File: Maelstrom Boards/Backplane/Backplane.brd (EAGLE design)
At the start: 254 x 101.6 mm, 10 parts, among them P3 39-30-04?_S

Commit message: Updated Backplane
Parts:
- added P1: 39-30-02?_S, con-molex-mini-fit:39-30-?02?
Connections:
- net 5V: now also P1.1
- net GND: now also P1.2
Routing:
- net 5V: track 269.1 -> 349.1 mm
- net GND: track 351.8 -> 425.8 mm
- net 3.3V: track 364.8 -> 360.3 mm
- net ROBOT_SCL: track 447.0 -> 442.9 mm
- net PLTA_ON/OFF: track 512.7 -> 515.1 mm, vias 1 -> 2
- net SWITCH_3: track 523.0 -> 521.9 mm
- net SWITCH_2: track 503.2 -> 502.3 mm
- net SWITCH_1: track 500.7 -> 499.9 mm
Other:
- board text added: "SPARE_2"
- board text added: "SPARE_3"
- board text added: "SPARE_4"
- board text added: "SPARE_5"
- board text added: "SPARE_6"
- board text added: "SPARE_7"

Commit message: Updated Backplane
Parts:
- moved P1 0.13 mm to (13.8, 90.7)
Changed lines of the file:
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@@
 <element name="U$3" library="5530843-6" package="5530843-6-BACKPLANEMATE" value="5530843-FEMALE" x="22.86" y="20.32" smashed="yes"/>
 <element name="U$4" library="5530843-6" package="5530843-6-BACKPLANEMATE" value="5530843-FEMALE" x="163.83" y="20.32" smashed="yes"/>
-<element name="P1" library="con-molex-mini-fit" package="39-30-?02?" value="39-30-02?_S" x="13.97" y="90.678" smashed="yes" rot="R270">
-<attribute name="NAME" x="0.2159" y="94.107" size="1.016" layer="25" ratio="18"/>
-<attribute name="VALUE" x="0.2159" y="85.979" size="1.016" layer="27" ratio="10"/>
+<element name="P1" library="con-molex-mini-fit" package="39-30-?02?" value="39-30-02?_S" x="13.843" y="90.678" smashed="yes" rot="R270">
+<attribute name="NAME" x="0.0889" y="94.107" size="1.016" layer="25" ratio="18"/>
+<attribute name="VALUE" x="0.0889" y="85.979" size="1.016" layer="27" ratio="10"/>
 </element>
 </elements>
@@
 <wire x1="73.025" y1="95.06780625" x2="72.31220625" y2="95.7806" width="1.016" layer="16"/>
 <wire x1="72.31220625" y1="95.7806" x2="29.6136" y2="95.7806" width="1.016" layer="16"/>
-<wire x1="21.971" y1="88.138" x2="16.51" y2="88.138" width="1.016" layer="16"/>
-<wire x1="16.51" y1="88.138" x2="13.97" y2="90.678" width="1.016" layer="16"/>
+<wire x1="21.971" y1="88.138" x2="16.383" y2="88.138" width="1.016" layer="16"/>
+<wire x1="16.383" y1="88.138" x2="13.843" y2="90.678" width="1.016" layer="16"/>
 <wire x1="29.6136" y1="95.7806" x2="21.971" y2="88.138" width="1.016" layer="16"/>
 </signal>
@@
 <wire x1="75.819" y1="89.535" x2="75.819" y2="95.758" width="1.016" layer="16"/>
 <wire x1="75.819" y1="95.758" x2="73.533" y2="98.044" width="1.016" layer="16"/>
-<wire x1="73.533" y1="98.044" x2="26.8478" y2="98.044" width="1.016" layer="16"/>
-<wire x1="26.8478" y1="98.044" x2="19.4818" y2="90.678" width="1.016" layer="16"/>
+<wire x1="73.533" y1="98.044" x2="26.7208" y2="98.044" width="1.016" layer="16"/>
+<wire x1="26.7208" y1="98.044" x2="19.3548" y2="90.678" width="1.016" layer="16"/>
 <wire x1="52.197" y1="6.604" x2="61.595" y2="6.604" width="1.016" layer="16"/>
 <via x="61.595" y="6.604" extent="1-16" drill="0.35"/>

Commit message: Updated Backplane
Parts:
- moved U$1 12.7 mm to (104.1, 81.3)
- moved U$3 12.7 mm to (35.6, 20.3)
- moved U$8 11.4 mm to (19.7, 7.37)
- moved U$2 1.27 mm to (231.1, 81.3)
- moved U$4 1.27 mm to (162.6, 20.3)
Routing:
- net GND: track 425.9 -> 458.0 mm
- net SPARE6: track 442.0 -> 423.1 mm
- net 5V: track 349.2 -> 368.1 mm
- net PWM_2: track 312.8 -> 330.8 mm, vias 5 -> 4
- net PWM_1: track 313.1 -> 330.8 mm, vias 5 -> 4
- net SPARE5: track 443.1 -> 425.5 mm
- net KILL_SWITCH: track 502.2 -> 488.1 mm, vias 7 -> 5
- net SWITCH_2: track 502.3 -> 489.2 mm
- net SWITCH_3: track 521.9 -> 509.7 mm
- net SPARE7: track 443.8 -> 432.1 mm
- net SWITCH_1: track 499.9 -> 488.7 mm
- net 3.3V: track 360.3 -> 349.2 mm
- net SWITCH_4: track 508.5 -> 501.0 mm
- net SPARE4: track 417.2 -> 411.3 mm
- net SPARE3: track 413.9 -> 408.5 mm
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
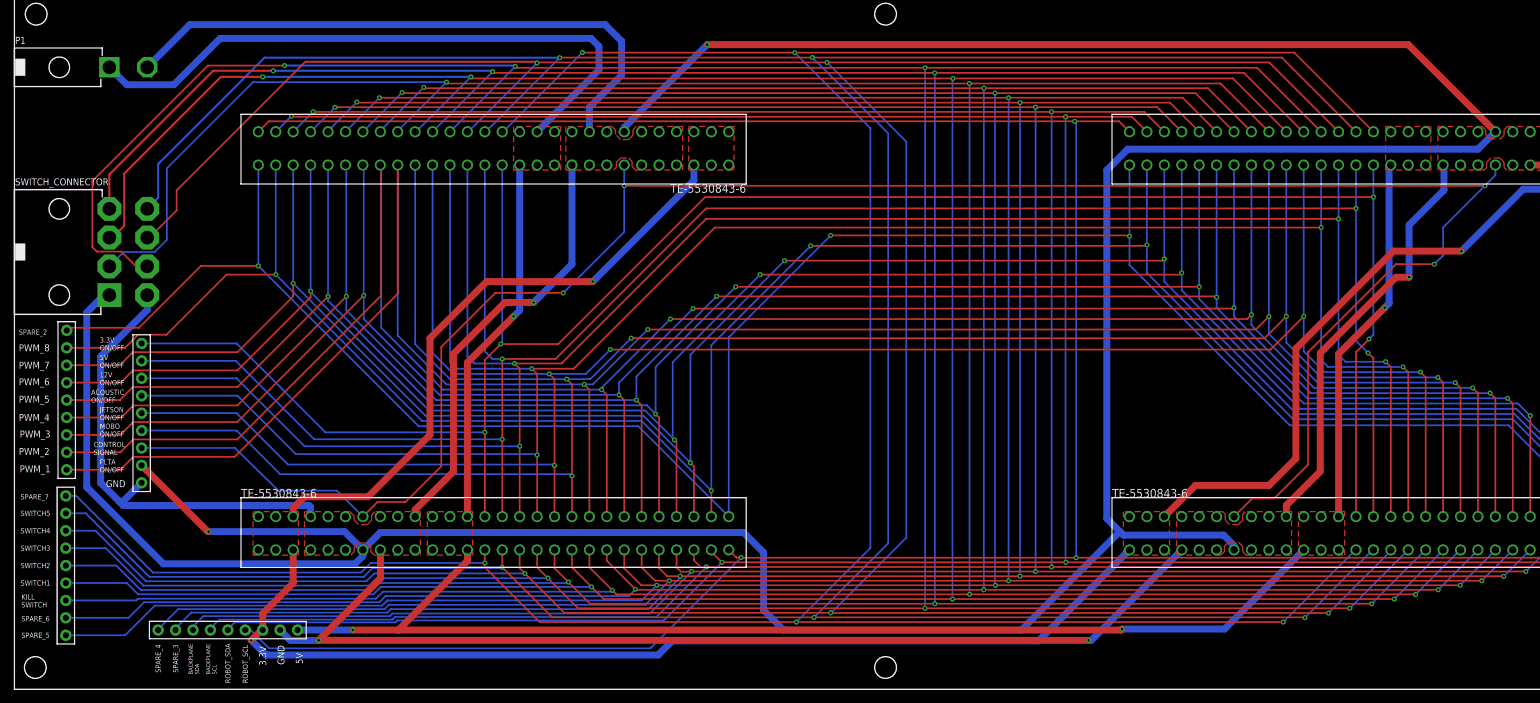
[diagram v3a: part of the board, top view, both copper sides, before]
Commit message: Finished Backplane
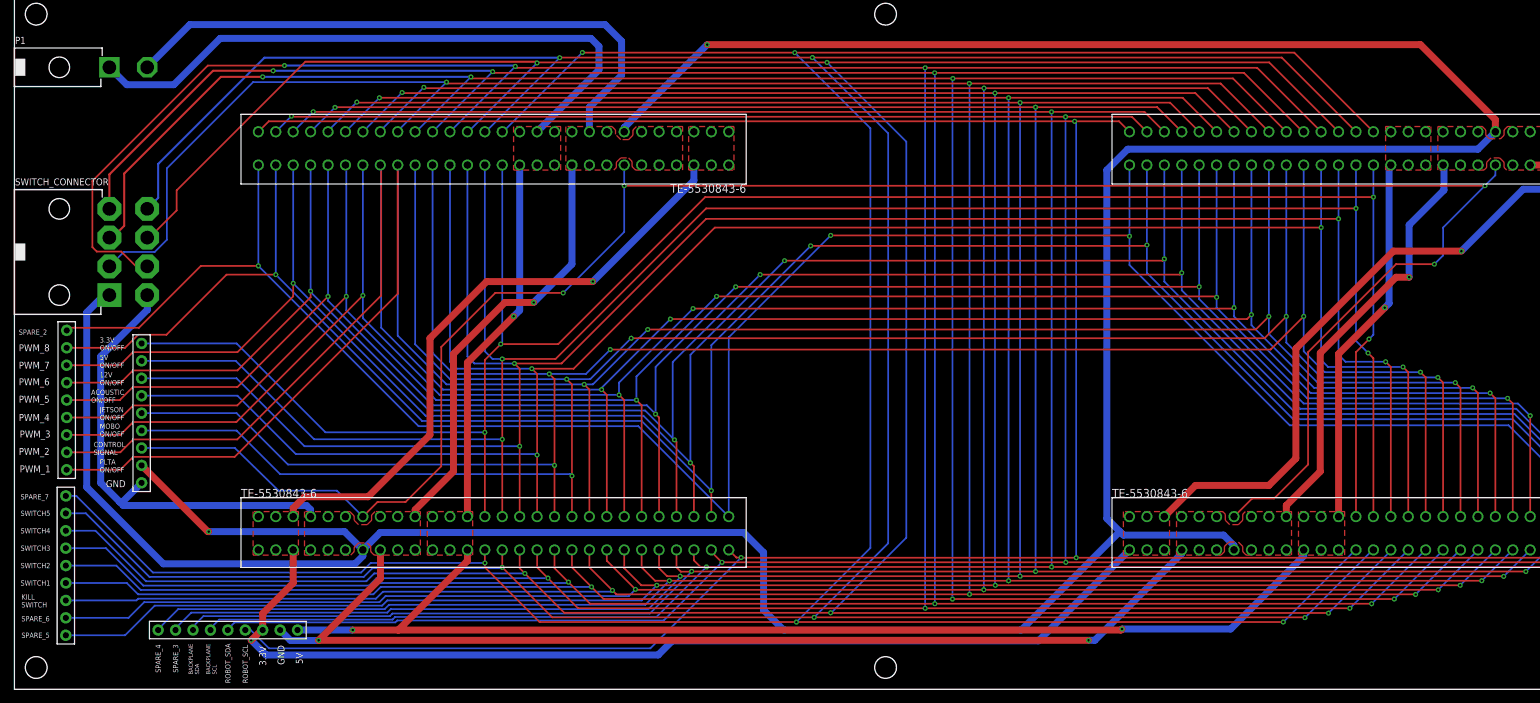
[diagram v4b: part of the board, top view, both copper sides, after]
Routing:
- net PLTA_ON/OFF: track 510.0 -> 511.1 mm
- net 5V: track 368.1 -> 368.6 mm
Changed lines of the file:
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@@
 <wire x1="0" y1="101.6" x2="0" y2="0" width="0" layer="20"/>
 <dimension x1="0" y1="101.6" x2="19.05" y2="101.6" x3="9.525" y3="77.851" textsize="1.778" layer="20" unit="inch"/>
-<dimension x1="254" y1="101.6" x2="247.65" y2="95.25" x3="250.825" y3="3.81" textsize="1.778" layer="20" dtype="horizontal" unit="inch"/>
+<dimension x1="254" y1="101.6" x2="250.825" y2="95.25" x3="252.4125" y3="3.81" textsize="1.778" layer="20" dtype="horizontal" unit="inch"/>
 <dimension x1="76.2" y1="83.82" x2="76.2" y2="78.74" x3="69.85" y3="81.28" textsize="1.778" layer="47" dtype="horizontal" unit="inch"/>
 <dimension x1="19.05" y1="91.44" x2="33.02" y2="86.36" x3="26.035" y3="77.851" textsize="1.778" layer="20" dtype="horizontal" unit="inch"/>
@@
 <dimension x1="0" y1="0" x2="0" y2="17.78" x3="254" y3="8.89" textsize="1.778" layer="47" dtype="horizontal" unit="inch"/>
 <hole x="3.175" y="98.425" drill="3.175"/>
-<hole x="3.048" y="3.175" drill="3.175"/>
+<hole x="3.175" y="3.175" drill="3.175"/>
 <hole x="250.825" y="3.175" drill="3.175"/>
 <hole x="250.825" y="98.425" drill="3.175"/>
@@
 <dimension x1="122.2375" y1="-1.143" x2="61.3664" y2="-1.143" x3="91.80195" y3="-25.146" textsize="1.778" layer="20" unit="inch" precision="4"/>
 <dimension x1="61.3664" y1="101.6" x2="51.8414" y2="101.6" x3="56.6039" y3="-24.638" textsize="1.778" layer="47" unit="inch" precision="3"/>
+<dimension x1="0" y1="0" x2="3.175" y2="0" x3="1.5875" y3="106.045" textsize="1.778" layer="20" unit="inch" precision="3"/>
 </plain>
 <attributes>
@@
 <via x="161.4678" y="8.7884" extent="1-16" drill="0.35"/>
 <wire x1="55.9562" y1="8.636" x2="49.3268" y2="8.636" width="1.016" layer="1"/>
-<wire x1="187.96" y1="20.32" x2="176.4284" y2="8.7884" width="1.016" layer="16"/>
-<wire x1="176.4284" y1="8.7884" x2="161.4678" y2="8.7884" width="1.016" layer="16"/>
+<wire x1="187.96" y1="20.32" x2="187.96" y2="19.431" width="1.016" layer="16"/>
+<wire x1="187.96" y1="19.431" x2="177.3174" y2="8.7884" width="1.016" layer="16"/>
+<wire x1="177.3174" y1="8.7884" x2="161.4678" y2="8.7884" width="1.016" layer="16"/>
 <wire x1="193.04" y1="25.1714" x2="193.04" y2="48.895" width="1.016" layer="1"/>
 <wire x1="193.04" y1="48.895" x2="199.771" y2="55.626" width="1.016" layer="1"/>
@@
 <via x="88.138" y="42.926" extent="1-16" drill="0.35"/>
 <wire x1="88.138" y1="42.926" x2="61.976" y2="42.926" width="0.254" layer="16"/>
-<wire x1="61.976" y1="42.926" x2="50.927" y2="53.975" width="0.254" layer="16"/>
+<wire x1="61.976" y1="42.926" x2="50.8" y2="54.102" width="0.254" layer="16"/>
 <via x="177.8" y="55.626" extent="1-16" drill="0.35"/>
 <wire x1="177.8" y1="55.626" x2="177.673" y2="55.499" width="0.254" layer="1"/>
@@
 <wire x1="88.138" y1="44.704" x2="88.138" y2="42.926" width="0.254" layer="16"/>
 <contactref element="U$6" pad="P$7"/>
-<via x="50.927" y="57.404" extent="1-16" drill="0.35"/>
-<wire x1="50.927" y1="53.975" x2="50.927" y2="57.404" width="0.254" layer="16"/>
+<via x="50.8" y="57.404" extent="1-16" drill="0.35"/>
+<wire x1="50.8" y1="54.102" x2="50.8" y2="57.404" width="0.254" layer="16"/>
 <contactref element="U$3" pad="22"/>
 <contactref element="U$1" pad="22"/>
 <contactref element="U$4" pad="22"/>
 <contactref element="U$2" pad="22"/>
-<wire x1="50.8" y1="76.4286" x2="50.927" y2="76.3016" width="0.254" layer="16"/>
-<wire x1="50.927" y1="76.3016" x2="50.927" y2="57.404" width="0.254" layer="16"/>
+<wire x1="50.8" y1="76.4286" x2="50.8" y2="57.404" width="0.254" layer="16"/>
 <wire x1="88.9" y1="25.1714" x2="88.9" y2="42.164" width="0.254" layer="1"/>
 <wire x1="215.9" y1="42.418" x2="215.9" y2="25.1714" width="0.254" layer="1"/>
 <wire x1="177.8" y1="76.4286" x2="177.8" y2="55.626" width="0.254" layer="16"/>
-<wire x1="32.4866" y1="38.9636" x2="17.31706875" y2="38.9636" width="0.254" layer="1"/>
-<wire x1="50.927" y1="57.404" x2="32.4866" y2="38.9636" width="0.254" layer="1"/>
+<wire x1="32.3596" y1="38.9636" x2="17.31706875" y2="38.9636" width="0.254" layer="1"/>
+<wire x1="50.8" y1="57.404" x2="32.3596" y2="38.9636" width="0.254" layer="1"/>
 <wire x1="15.43746875" y1="37.084" x2="7.62" y2="37.084" width="0.254" layer="1"/>
 <wire x1="17.31706875" y1="38.9636" x2="15.43746875" y2="37.084" width="0.254" layer="1"/>
@@
 <contactref element="U$7" pad="P$9"/>
 <contactref element="U$8" pad="P$8"/>
-<wire x1="42.9514" y1="26.797" x2="15.875" y2="26.797" width="1.016" layer="16"/>
+<wire x1="42.5704" y1="26.797" x2="15.875" y2="26.797" width="1.016" layer="16"/>
 <wire x1="15.367" y1="27.305" x2="15.748" y2="27.305" width="1.016" layer="16"/>
 <wire x1="15.875" y1="26.797" x2="15.367" y2="27.305" width="1.016" layer="16"/>
@@
 <wire x1="12.573" y1="30.099" x2="12.573" y2="48.514" width="1.016" layer="16"/>
 <wire x1="12.573" y1="48.514" x2="19.3802" y2="55.3212" width="1.016" layer="16"/>
-<wire x1="42.9514" y1="26.797" x2="43.18" y2="26.5684" width="1.016" layer="16"/>
+<wire x1="42.5704" y1="26.797" x2="43.18" y2="26.1874" width="1.016" layer="16"/>
 <wire x1="18.542" y1="30.099" x2="15.748" y2="27.305" width="1.016" layer="16"/>
 <contactref element="U$1" pad="6"/>
@@
 <contactref element="U$2" pad="47"/>
 <wire x1="220.98" y1="76.4286" x2="223.52" y2="76.4286" width="1.016" layer="1"/>
-<wire x1="43.18" y1="26.5684" x2="43.18" y2="25.1714" width="1.016" layer="16"/>
+<wire x1="43.18" y1="26.1874" x2="43.18" y2="25.1714" width="1.016" layer="16"/>
 <wire x1="53.3654" y1="16.1544" x2="53.3654" y2="20.2946" width="1.016" layer="1"/>
 <wire x1="44.3484" y1="7.1374" x2="53.3654" y2="16.1544" width="1.016" layer="1"/>
 <via x="156.591" y="7.1374" extent="1-16" drill="0.35"/>
-<wire x1="170.18" y1="20.32" x2="156.9974" y2="7.1374" width="1.016" layer="16"/>
-<wire x1="156.9974" y1="7.1374" x2="156.591" y2="7.1374" width="1.016" layer="16"/>
+<wire x1="170.18" y1="20.32" x2="170.18" y2="19.812" width="1.016" layer="16"/>
+<wire x1="170.18" y1="19.812" x2="157.5054" y2="7.1374" width="1.016" layer="16"/>
+<wire x1="157.5054" y1="7.1374" x2="156.591" y2="7.1374" width="1.016" layer="16"/>
 <wire x1="156.591" y1="7.1374" x2="44.3484" y2="7.1374" width="1.016" layer="1"/>
 <wire x1="185.42" y1="25.1714" x2="185.42" y2="26.797" width="1.016" layer="1"/>
@@
 <wire x1="88.9" y1="81.8896" x2="88.9" y2="81.28" width="1.016" layer="16"/>
 <via x="100.9904" y="93.98" extent="1-16" drill="0.35"/>
-<wire x1="203.2" y1="93.98" x2="100.9904" y2="93.98" width="1.016" layer="1"/>
-<wire x1="203.2" y1="93.98" x2="215.9" y2="81.28" width="1.016" layer="1"/>
+<wire x1="204.978" y1="93.98" x2="100.9904" y2="93.98" width="1.016" layer="1"/>
+<wire x1="215.9" y1="83.058" x2="215.9" y2="81.28" width="1.016" layer="1"/>
+<wire x1="215.9" y1="83.058" x2="204.978" y2="93.98" width="1.016" layer="1"/>
 <wire x1="215.9" y1="81.28" x2="213.36" y2="78.74" width="1.016" layer="16"/>
 <wire x1="213.36" y1="78.74" x2="162.306" y2="78.74" width="1.016" layer="16"/>

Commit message: Added pull-up resistors to backplane
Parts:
- added R1, R10, R11, R12, R13, R14, R2, R3, R4, R5, R6, R7, R8, R9: (no value), rcl:R0603
- added R15, R16, R17, R18: 4.7k, rcl:R0603
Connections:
- net 3.3V: now also R10.1, R11.1, R12.1, R13.1, R14.1, R15.1, R16.1, R17.1, R18.1, R9.1
- net 5V: now also R1.1, R2.1, R3.1, R4.1, R5.1, R6.1, R7.1, R8.1
- net BACKPLANE_SCL: now also R16.2
- net BACKPLANE_SDA: now also R15.2
- net KILL_SWITCH: now also R9.2
- net PWM_1: now also R1.2
- net PWM_2: now also R2.2
- net PWM_3: now also R3.2
- net PWM_4: now also R4.2
- net PWM_5: now also R5.2
- net PWM_6: now also R6.2
- net PWM_7: now also R7.2
- net PWM_8: now also R8.2
- net ROBOT_SCL: now also R18.2
- net ROBOT_SDA: now also R17.2
- net SWITCH_1: now also R10.2
- net SWITCH_2: now also R11.2
- net SWITCH_3: now also R12.2
- net SWITCH_4: now also R13.2
- net SWITCH_5: now also R14.2
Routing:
- net 3.3V: track 349.2 -> 409.3 mm
- net 5V: track 368.6 -> 414.2 mm
- net PWM_8: track 318.3 -> 338.7 mm
- net PWM_7: track 317.8 -> 334.3 mm
- net PWM_6: track 316.3 -> 329.4 mm
- net PWM_5: track 314.4 -> 324.5 mm
- net PWM_1: track 330.8 -> 338.5 mm
- net PWM_4: track 313.5 -> 321.3 mm
- net PWM_3: track 312.3 -> 319.8 mm
- net PWM_2: track 330.8 -> 338.1 mm
- net KILL_SWITCH: track 488.1 -> 492.8 mm
- net SWITCH_5: track 503.5 -> 508.1 mm
- net BACKPLANE_SDA: track 405.4 -> 409.8 mm
- net SWITCH_1: track 488.7 -> 493.0 mm
- net SWITCH_4: track 501.0 -> 505.3 mm
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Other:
- board size 254 x 101.6 mm -> 254 x 101.7 mm
